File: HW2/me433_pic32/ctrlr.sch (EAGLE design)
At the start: 22 parts, among them J1 USB-MINI-B, J2 HEADER-6, J3 HEADER-8, J4 HEADER-8, U1 PIC32MX250F128B, X1 CSTLS8M00G53

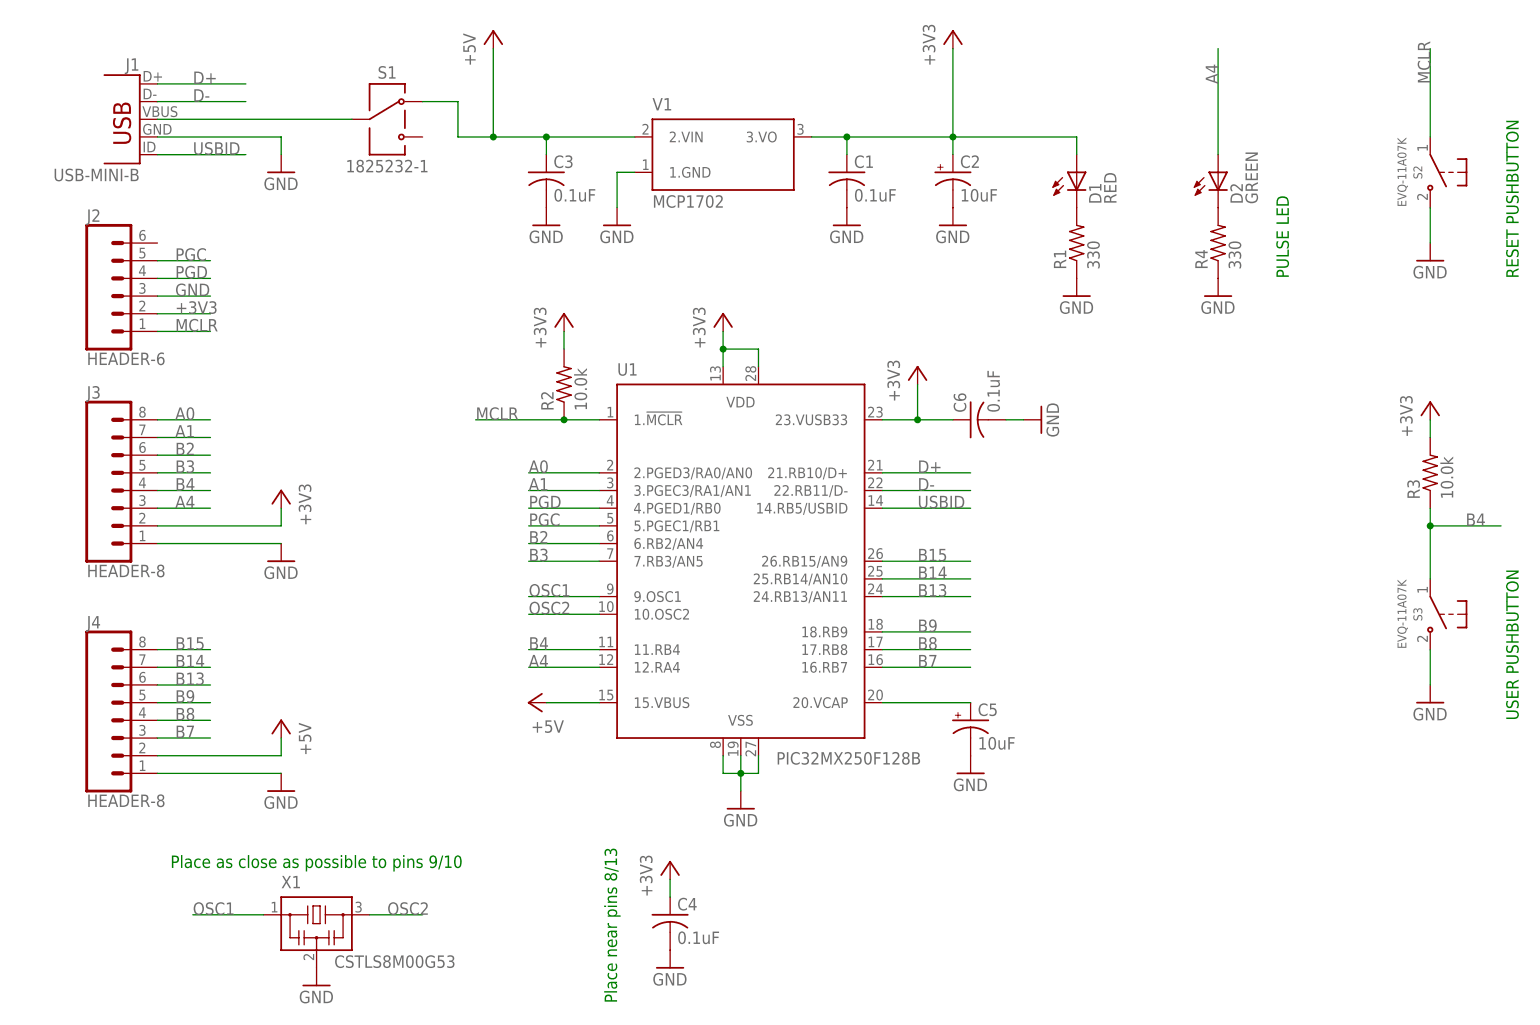
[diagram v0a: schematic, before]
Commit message: Added Gerbers for HW3, tweaked board layout and saved as Rev2. Not happy on the hole sizing on the layout (thanks Eagle) so I may come back and make those larger for standard standoffs.
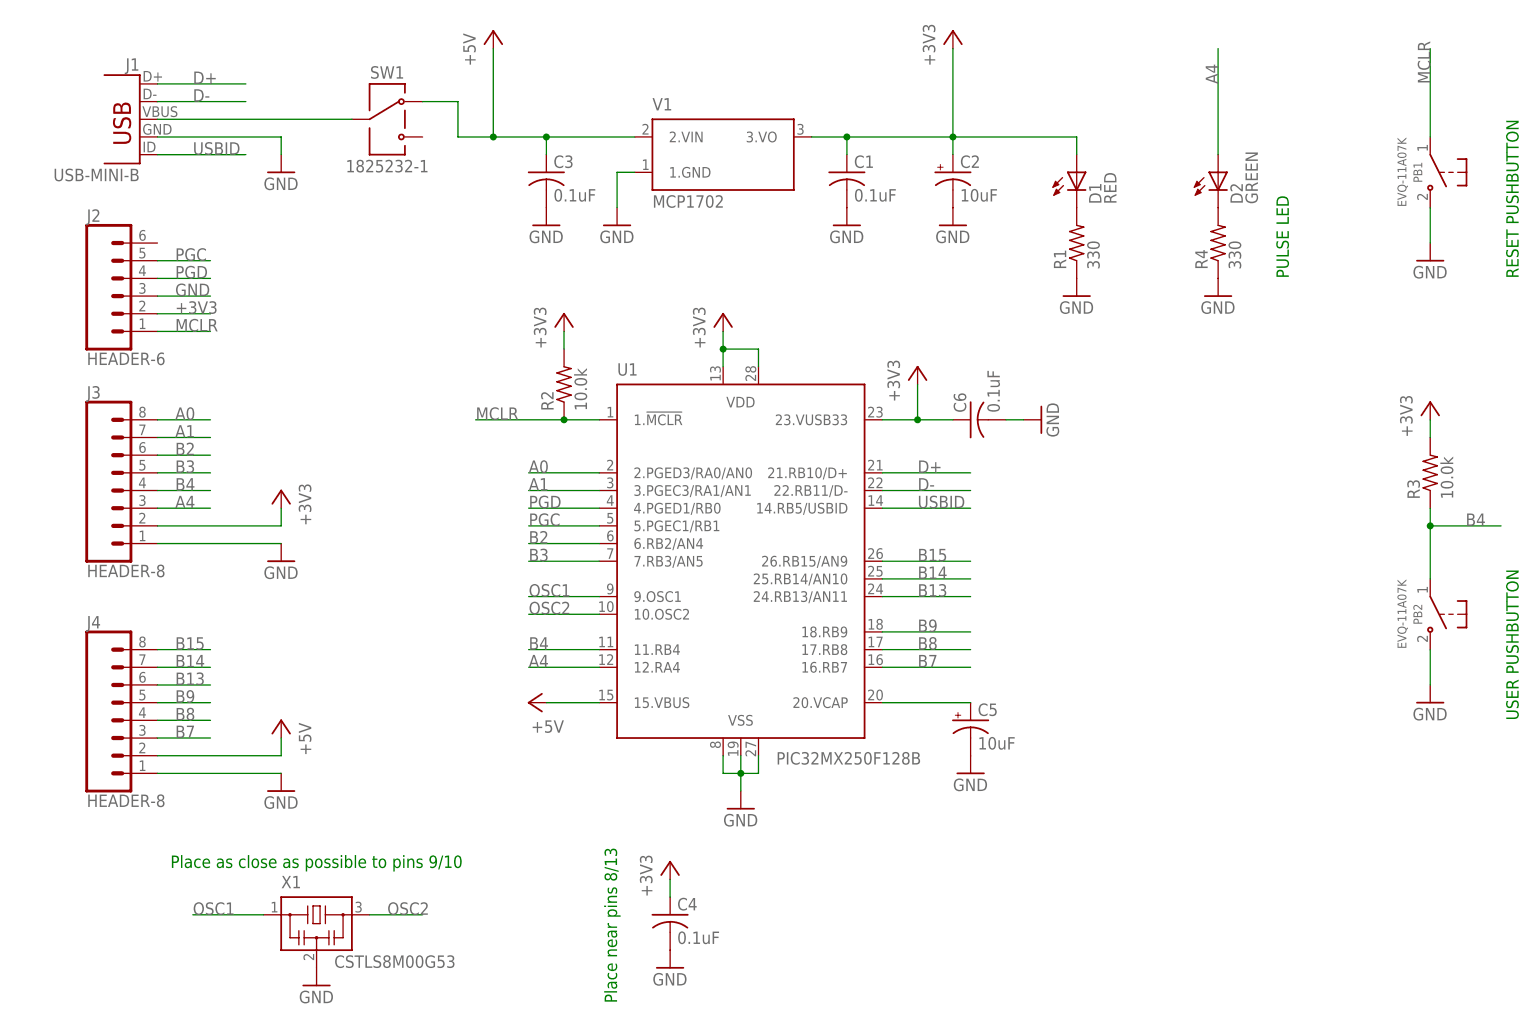
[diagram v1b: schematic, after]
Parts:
- renumbered S1 to SW1, S2 to PB1, S3 to PB2
